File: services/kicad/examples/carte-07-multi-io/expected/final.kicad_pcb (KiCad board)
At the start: 2 copper layers, 47.6 x 38.7 mm, 44 parts, among them J1 IN_5V, J10 IO0, J11 IO1, J12 IO2, J2 SWD, U1 STM32F103C8T6, U2 AMS1117-3.3

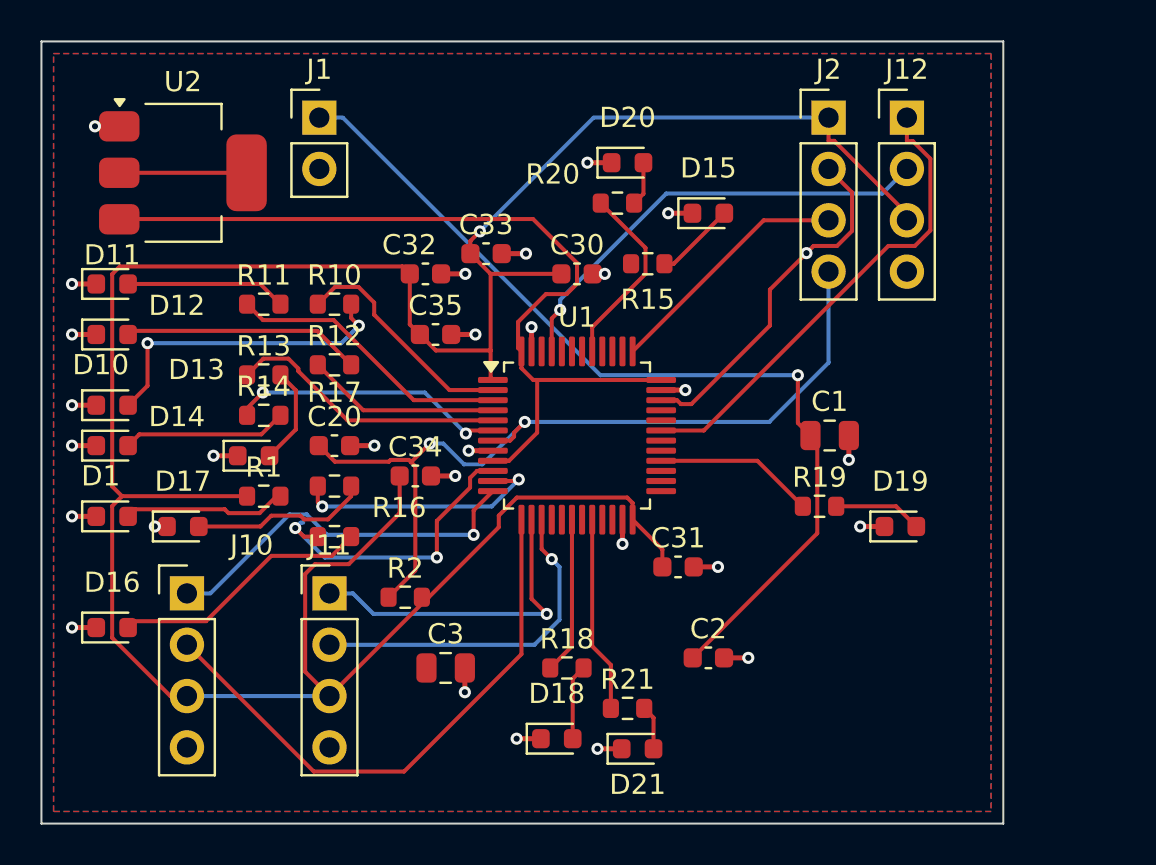
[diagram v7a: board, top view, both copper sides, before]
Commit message: feat(routing): routage prioritaire des liaisons critiques, et une pastille un proprietaire
D-2026-09-25-a (validee : « propose toi et fais tout selon votre
recommandation »). Avant Freerouting, tools/nets_critiques.py detecte par la
topologie les liaisons critiques - quartz, charges du quartz, decouplages -
et l'operation runner relier_liaisons les pose par des pistes courtes, sur
une face, sans via, en evitant les vias reserves. Elles sont protegees avec
la liaison GND. Limite : corps a 3 mm au plus (comme le cluster natif) et
piste a 6 mm au plus. Paires differentielles detectees, jamais routees.
Desactive par defaut (reglage routage_prioritaire) jusqu'a la mesure A/B,
un tirage sur deux quand il est actif.

Mesure de detection : 2 a 9 decouplages par carte, aucun quartz retenu -
ils sont a 9-27 mm des broches OSC. Le defaut dominant est le placement.

Etape 0, deux corrections du DSN envoye a Freerouting :
- une pastille, un proprietaire : un via reserve a moins de 0,5 mm d'un via
  protege est ecarte avec son troncon, et un element protege ecrit deux
  fois ne l'est qu'une (4 vias au meme point mesures : 7 s -> 220 s et plus,
  puis HTTP 500 en production) ;
- fuite d'etat : en entrant dans un palier sans protection voulue, la
  liaison GND du palier precedent restait protegee.

D-2026-09-24-g : chaque palier repart libre (le tirage protege echouait a
chaque changement de palier). carte-07 livree : 100 %, 4 couches, 0 erreur,
aucun court-circuit vs schema.

Co-Authored-By: Claude Opus 5.5 <noreply@anthropic.com>
Claude-Session: https://claude.ai/code/session_01TnMqm4La2CxQHHB5K8aSSV
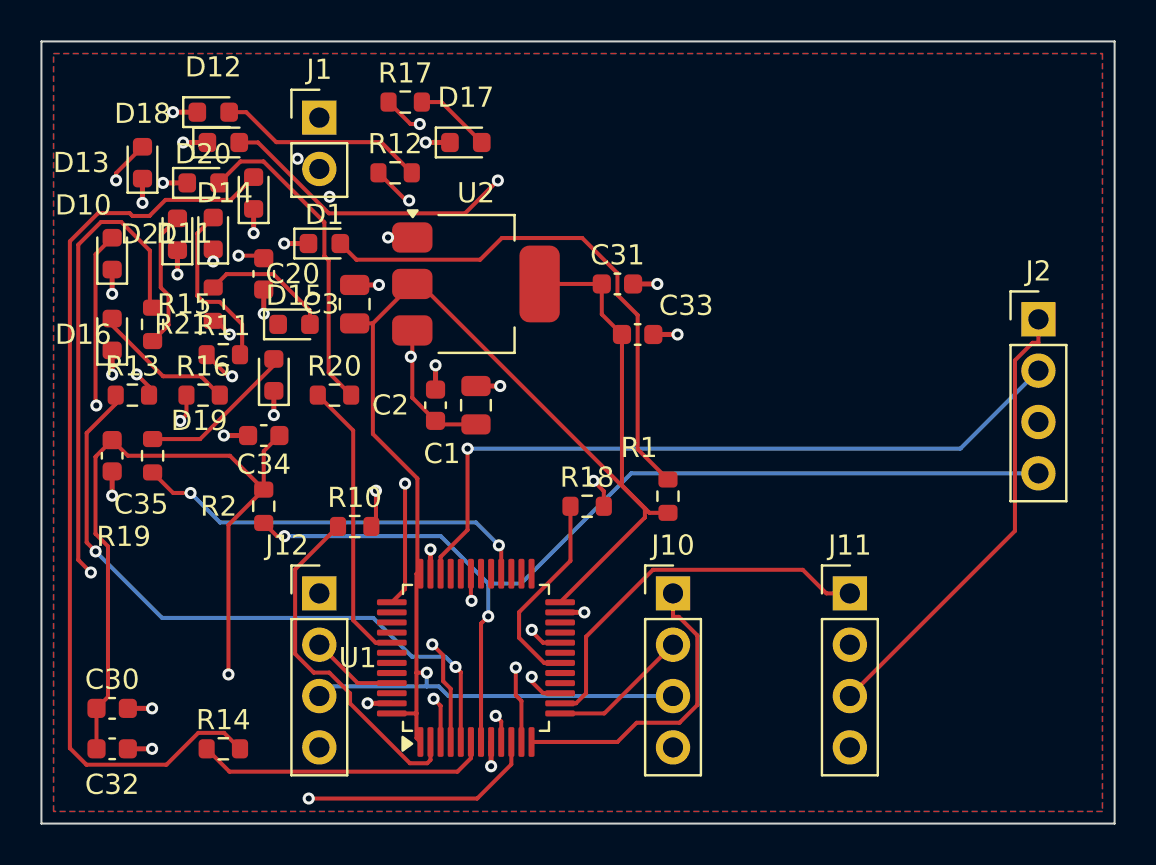
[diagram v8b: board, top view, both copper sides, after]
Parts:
- moved J12 37.4 mm to (107.2, 92.3)
- moved D21 34.2 mm to (100.2, 74.5), turned to 90 degrees
- moved D18 33.8 mm to (102.5, 70.0)
- moved R19 33.1 mm to (99.0, 85.5), turned to 90 degrees
- moved D19 31.9 mm to (105.0, 81.5), turned to 90 degrees
- moved C30 31.5 mm to (97.0, 98.0)
- moved R21 30.2 mm to (99.0, 79.0), turned to -90 degrees
- moved C32 28.2 mm to (97.0, 100.0)
- moved J11 25.7 mm to (133.5, 92.3)
- moved J10 24.0 mm to (124.8, 92.3)
- moved D17 23.6 mm to (114.5, 70.0)
- moved R15 21.6 mm to (102.0, 78.0), turned to 90 degrees
- moved D15 21.2 mm to (106.0, 79.0)
- moved D20 21.0 mm to (101.5, 72.0)
- moved R1 20.0 mm to (124.5, 87.5), turned to 90 degrees
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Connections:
- C3 pad 1: Net-(C3-1) -> +3V3
- U1 pad 36: PWR_FLAG -> +3V3
- U1 pad 48: PWR_FLAG -> +3V3
- U1 pad 9: PWR_FLAG -> IO_L5
- U2 pad 2: Net-(U2-2) -> +3V3
- U2 pad 3: PWR_FLAG -> VIN
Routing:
- net PWR_FLAG: track 43.2 -> 0.00 mm
- net IO_L11: track 9.72 -> 48.7 mm, vias 0 -> 2
- net LEDA4: track 8.16 -> 45.3 mm
- net LEDA8: track 3.72 -> 33.2 mm, vias 0 -> 2
- net IO_L5: track 0.00 -> 27.2 mm, vias 0 -> 2
- net SWCLK: track 12.4 -> 38.7 mm, vias 0 -> 1
- net VIN: track 45.9 -> 21.0 mm
- net NRST: track 42.4 -> 66.8 mm, vias 2 -> 3
- net +3V3: track 134.3 -> 158.5 mm, vias 1 -> 2
- net IO_L7: track 12.7 -> 34.8 mm
- net EXT0_2: track 28.2 -> 7.00 mm
- net IO_L2: track 9.59 -> 30.2 mm, vias 0 -> 2
- net IO_L6: track 15.3 -> 34.6 mm
- net SWDIO: track 17.7 -> 36.6 mm
- net IO_L3: track 13.8 -> 32.5 mm, vias 0 -> 2
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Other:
- board size 47.6 x 38.7 mm -> 53.1 x 38.7 mm
- copper layers 2 -> 4
